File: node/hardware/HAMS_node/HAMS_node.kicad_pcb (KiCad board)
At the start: 2 copper layers, 76.1 x 40.1 mm, 41 parts, among them J1 Conn_01x02, J2 Conn_02x07_Odd_Even, J3 Conn_01x04, J4 Conn_01x04, J5 Conn_01x04, J6 Conn_01x04, J7 Conn_01x08, Q1 DMP3099L, SW1 TL3305BF100QG, SW2 TL3305BF100QG, U1 STM32L031K6Tx, U2 NRF24L01_Breakout, U3 nRF24L01p SMD module, Y1 CM9V-T1A

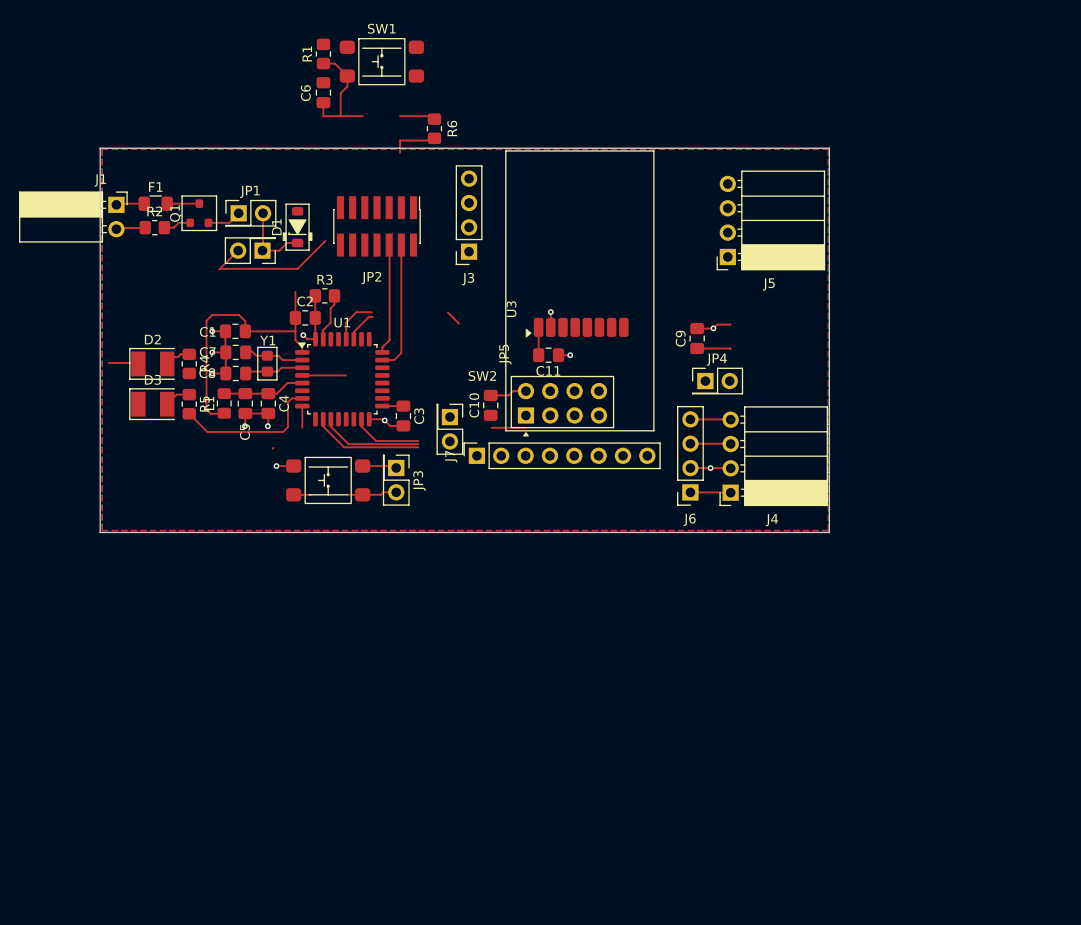
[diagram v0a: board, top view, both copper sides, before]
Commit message: Improve HAMS node HW: PCB and device resize
Change many 0805 devices for 0603 devices.
Add mounting holes.
Make the board 4.5 x 5 cm size.
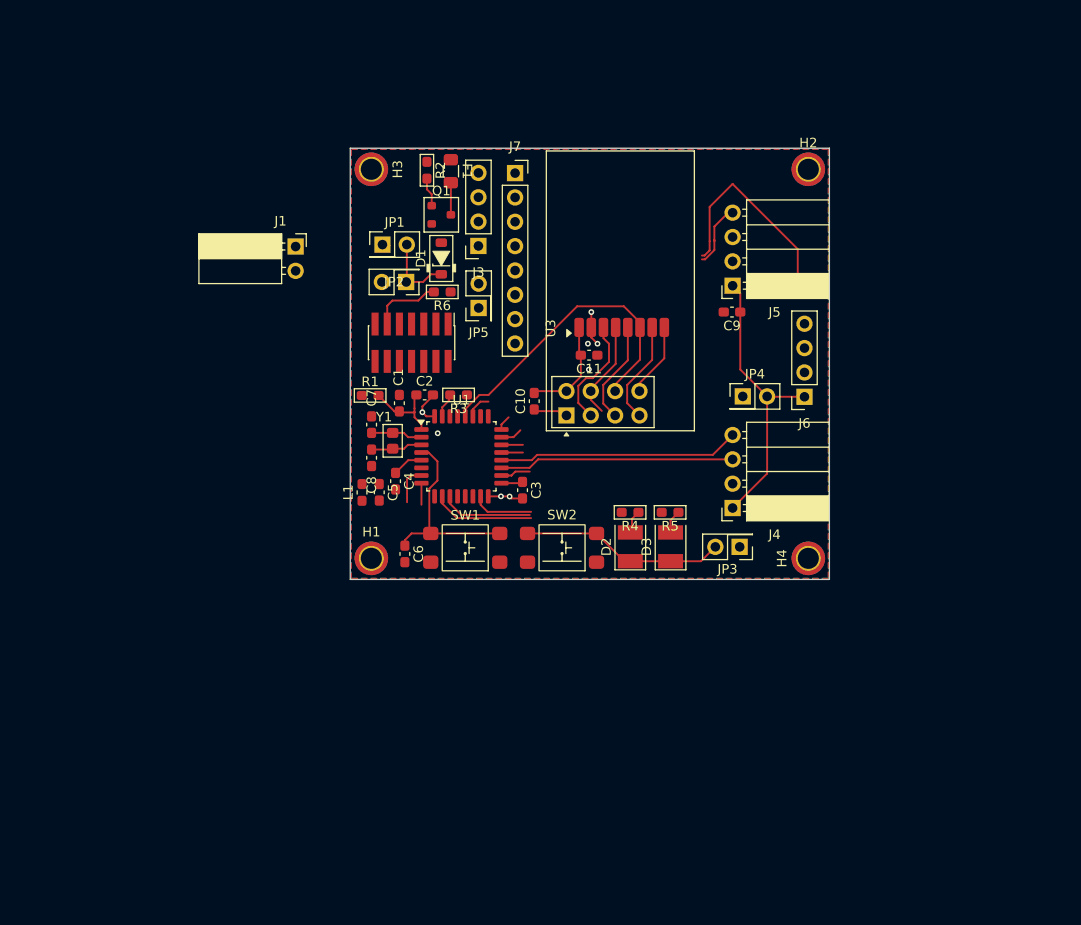
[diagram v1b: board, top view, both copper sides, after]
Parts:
- added H1: MountingHole_Pad, MountingHole:MountingHole_2.2mm_M2_ISO7380_Pad_TopBottom, F.Cu at (142.3, 71.4)
- added H2: MountingHole_Pad, MountingHole:MountingHole_2.2mm_M2_ISO7380_Pad_TopBottom, F.Cu at (187.9, 30.8)
- added H3: MountingHole_Pad, MountingHole:MountingHole_2.2mm_M2_ISO7380_Pad_TopBottom, F.Cu at (142.3, 30.8)
- added H4: MountingHole_Pad, MountingHole:MountingHole_2.2mm_M2_ISO7380_Pad_TopBottom, F.Cu at (187.9, 71.4)
- C1, C10, C11, C2, C3, C4, C5, C6, C7, C8, C9: footprint Capacitor_SMD:C_0805_2012Metric_Pad1.18x1.45mm_HandSolder -> Capacitor_SMD:C_0603_1608Metric_Pad1.08x0.95mm_HandSolder
- L1: footprint Inductor_SMD:L_0805_2012Metric_Pad1.15x1.40mm_HandSolder -> Inductor_SMD:L_0603_1608Metric_Pad1.05x0.95mm_HandSolder
- R1, R2, R3, R4, R5, R6: footprint Resistor_SMD:R_0805_2012Metric_Pad1.20x1.40mm_HandSolder -> PCM_Resistor_SMD_AKL:R_0603_1608Metric_Pad1.05x0.95mm_HandSolder
- moved D3 56.0 mm to (173.5, 70.2), turned to 90 degrees
- moved D2 53.4 mm to (169.3, 70.2), turned to 90 degrees
- moved SW1 51.5 mm to (152.1, 70.3), turned to 180 degrees
- moved R5 51.4 mm to (173.5, 66.6), turned to 180 degrees
- moved C6 48.9 mm to (145.8, 70.9), turned to -90 degrees
- moved R4 48.5 mm to (169.3, 66.6), turned to 180 degrees
- moved JP3 36.8 mm to (180.7, 70.2), turned to 180 degrees
- moved R1 36.0 mm to (142.2, 54.4), turned to 0 degrees
- moved F1 31.0 mm to (150.6, 31.0), turned to -90 degrees
- moved J7 29.8 mm to (157.3, 31.2), turned to 0 degrees
- moved R2 29.0 mm to (148.1, 30.9), turned to -90 degrees
- moved SW2 25.4 mm to (162.2, 70.3), turned to 180 degrees
- moved Q1 25.3 mm to (149.6, 35.5), turned to 0 degrees
- moved J1 19.2 mm to (134.4, 38.9)
- moved C1 18.7 mm to (145.2, 55.2), turned to 90 degrees
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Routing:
- net /I2C_SDA: track 4.21 -> 55.8 mm
- net GND: track 51.7 -> 14.9 mm, vias 12 -> 8
- net /VDD_MCU: track 46.0 -> 10.5 mm
- net /SPI_MOSI: track 4.87 -> 32.4 mm
- net /VDD_SENSOR: track 7.73 -> 30.1 mm
- net /I2C_SCL: track 4.21 -> 24.5 mm
- net /nRF24_CE: track 0.75 -> 15.6 mm
- net /LED_RED: track 15.6 -> 4.06 mm
- net Net-(D2-K): track 10.1 -> 21.4 mm
- net /SWDIO: track 13.6 -> 2.28 mm
- net /SPI_MISO: track 3.38 -> 13.5 mm
- net /SWCLK: track 11.5 -> 1.59 mm
- net /SPI_SCK: track 10.6 -> 20.3 mm
- net /nRF24_CSN: track 11.7 -> 20.9 mm
- net /nRF24_IRQ: track 7.31 -> 14.2 mm
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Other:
- board size 76.1 x 40.1 mm -> 50 x 45 mm

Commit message: Improve HAMS node HW: PCB resize, optimization
Optimize MCU pinout with respect to PCB routing.
Change PCB size to 47.5 mm x 50 mm.
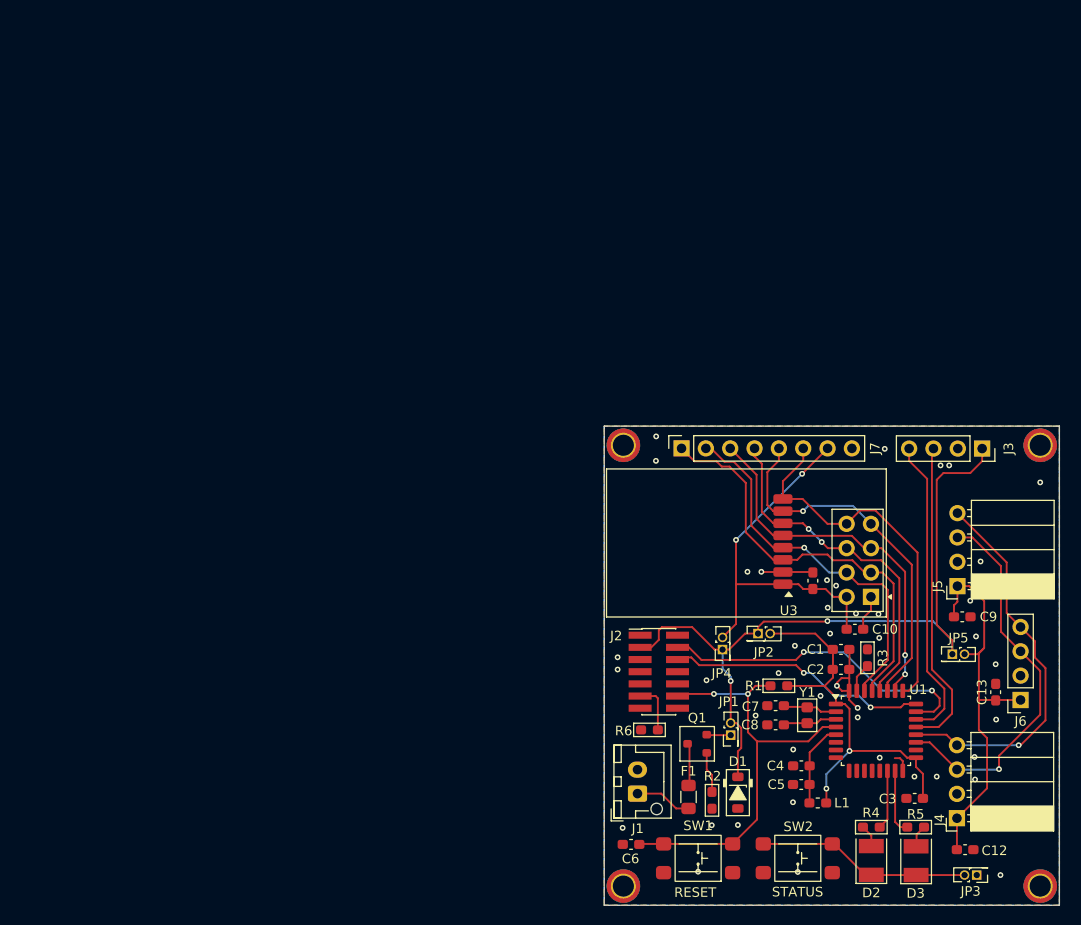
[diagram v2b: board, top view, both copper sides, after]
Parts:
- added C12: 10 uF, Capacitor_SMD:C_0603_1608Metric_Pad1.08x0.95mm_HandSolder, F.Cu at (204.3, 101.8)
- added C13: 10 uF, Capacitor_SMD:C_0603_1608Metric_Pad1.08x0.95mm_HandSolder, F.Cu at (207.4, 85.4)
- J1: footprint Connector_PinSocket_2.54mm:PinSocket_1x02_P2.54mm_Horizontal -> Connector_JST:JST_XH_B2B-XH-AM_1x02_P2.50mm_Vertical
- JP1, JP2, JP3: footprint Connector_PinHeader_2.54mm:PinHeader_2x01_P2.54mm_Vertical -> Connector_PinHeader_1.27mm:PinHeader_2x01_P1.27mm_Vertical
- JP4: renamed from JP5; footprint Connector_PinHeader_2.54mm:PinHeader_2x01_P2.54mm_Vertical -> Connector_PinHeader_1.27mm:PinHeader_2x01_P1.27mm_Vertical
- JP5: renamed from JP4; footprint Connector_PinHeader_2.54mm:PinHeader_2x01_P2.54mm_Vertical -> Connector_PinHeader_1.27mm:PinHeader_2x01_P1.27mm_Vertical
- Y1: footprint PCM_Crystal_Handsoldering_AKL:Crystal_SMD_MicroCrystal_CM9V-T1A-2Pin_1.6x1.0mm_BigPads -> PCM_Crystal_AKL:Crystal_SMD_MicroCrystal_CM9V-T1A-2Pin_1.6x1.0mm_BigPads
- moved H2 78.6 mm to (212.1, 105.6), turned to 45 degrees
- moved H3 75.5 mm to (212.1, 59.6), turned to 45 degrees
- moved R2 72.2 mm to (177.8, 96.7), turned to 90 degrees
- moved F1 69.9 mm to (175.4, 96.3), turned to 90 degrees
- moved J1 67.3 mm to (170.1, 96.0), turned to 90 degrees
- moved D1 63.8 mm to (180.6, 95.8), turned to -90 degrees
- moved JP1 62.8 mm to (179.8, 89.8), turned to 90 degrees
- moved Q1 61.3 mm to (176.3, 90.8), turned to 180 degrees
- moved L1 57.6 mm to (188.9, 96.9), turned to 180 degrees
- moved J3 56.7 mm to (206.0, 59.9), turned to -90 degrees
- moved C5 53.6 mm to (187.2, 95.0), turned to 180 degrees
- moved C1 52.8 mm to (191.3, 80.9), turned to 0 degrees
- moved R1 52.3 mm to (184.8, 84.7)
- moved C3 52.1 mm to (199.0, 96.5), turned to 180 degrees
- moved C2 52.0 mm to (191.3, 83.0)
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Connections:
- J7 pad 1: /nRF24_CSN -> /nRF24_CE
- J7 pad 2: /nRF24_CE -> /nRF24_CSN
- J7 pad 3: /nRF24_IRQ -> /SPI_SCK
- J7 pad 4: /SPI_SCK -> /SPI_MOSI
- J7 pad 6: /SPI_MOSI -> /nRF24_IRQ
- U1 pad 10: /nRF24_CSN -> unconnected-(U1-PA4-Pad10)
- U1 pad 11: /SPI_SCK -> unconnected-(U1-PA5-Pad11)
- U1 pad 14: unconnected-(U1-PB0-Pad14) -> /LED_GREEN
- U1 pad 15: /nRF24_IRQ -> /LED_RED
- U1 pad 18: /nRF24_CE -> unconnected-(U1-PA8-Pad18)
- U1 pad 25: unconnected-(U1-PA15-Pad25) -> /nRF24_IRQ
- U1 pad 26: unconnected-(U1-PB3-Pad26) -> /SPI_SCK
- U1 pad 29: unconnected-(U1-PB6-Pad29) -> /nRF24_CE
- U1 pad 30: unconnected-(U1-PB7-Pad30) -> /nRF24_CSN
- U1 pad 7: /LED_RED -> unconnected-(U1-PA1-Pad7)
- U1 pad 8: /LED_GREEN -> unconnected-(U1-PA2-Pad8)
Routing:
- net VDD: track 7.92 -> 79.4 mm, vias 0 -> 2
- net /SWDIO: track 2.28 -> 34.4 mm, vias 0 -> 2
- net /VDD_MCU: track 10.5 -> 41.9 mm, vias 0 -> 2
- net /GPIO_0: track 2.24 -> 32.9 mm
- net /GPIO_1: track 2.24 -> 32.1 mm
- net /VDD_nRF24: track 10.9 -> 39.4 mm, vias 0 -> 2
- net /nRF24_CE: track 15.6 -> 43.6 mm
- net /SWCLK: track 1.59 -> 27.7 mm, vias 0 -> 2
- net /NRST: track 20.8 -> 46.1 mm, vias 0 -> 2
- net /SPI_MISO: track 13.5 -> 38.7 mm, vias 0 -> 1
- net /nRF24_IRQ: track 14.2 -> 39.4 mm
- net /SPI_SCK: track 20.3 -> 39.1 mm, vias 0 -> 2
- net /nRF24_CSN: track 20.9 -> 39.5 mm, vias 0 -> 1
- net /I2C_SCL: track 24.5 -> 40.4 mm, vias 0 -> 1
- net /I2C_SDA: track 55.8 -> 40.5 mm, vias 0 -> 1
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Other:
- board size 50 x 45 mm -> 47.5 x 50 mm
- board text added: "RESET"
- board text added: "STATUS"

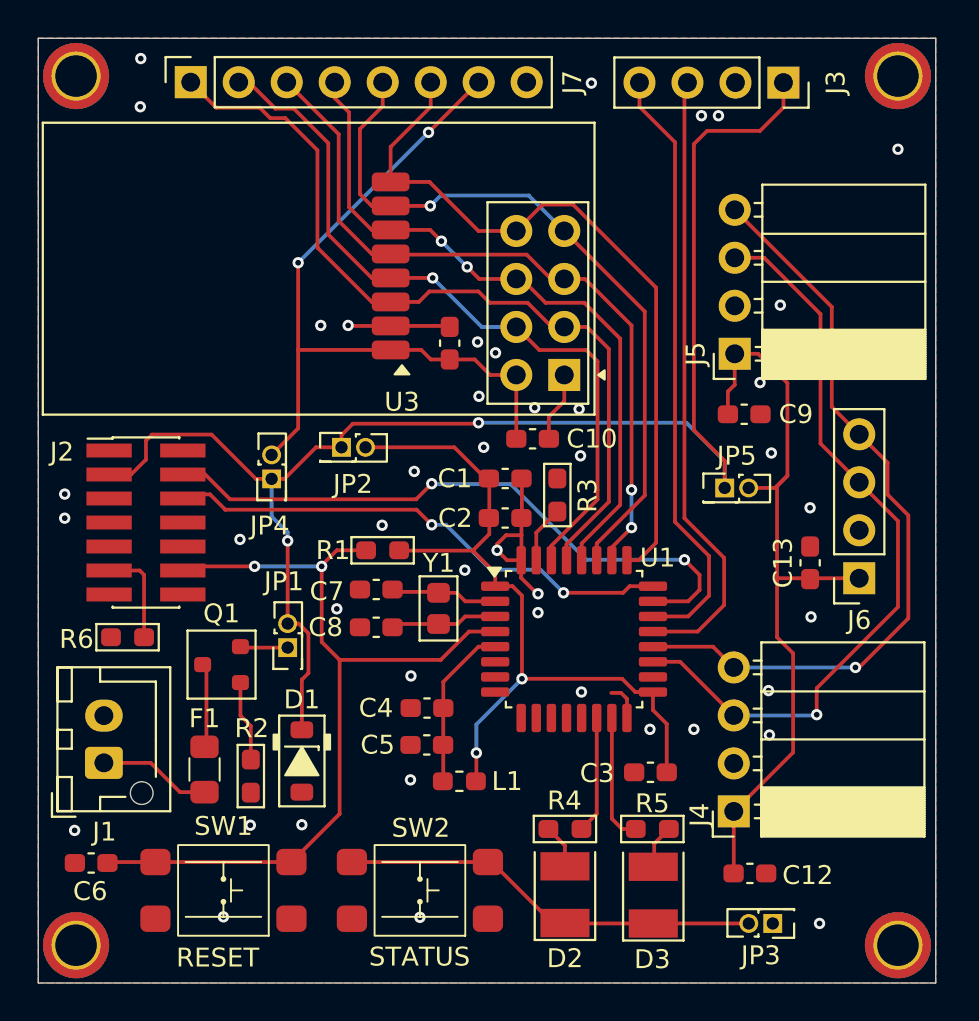
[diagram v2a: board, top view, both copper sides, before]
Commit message: Improve HAMS node HW: schematic and PCB
Change LED section (compact LED, DPDT switch).
Remove VDDA ferrite bead and bulk capacitor.
Add pads for I2C pullups.
Add silkscreen labels.
Update footprints of custom symbols.
Change mounting holes to non-grounded.
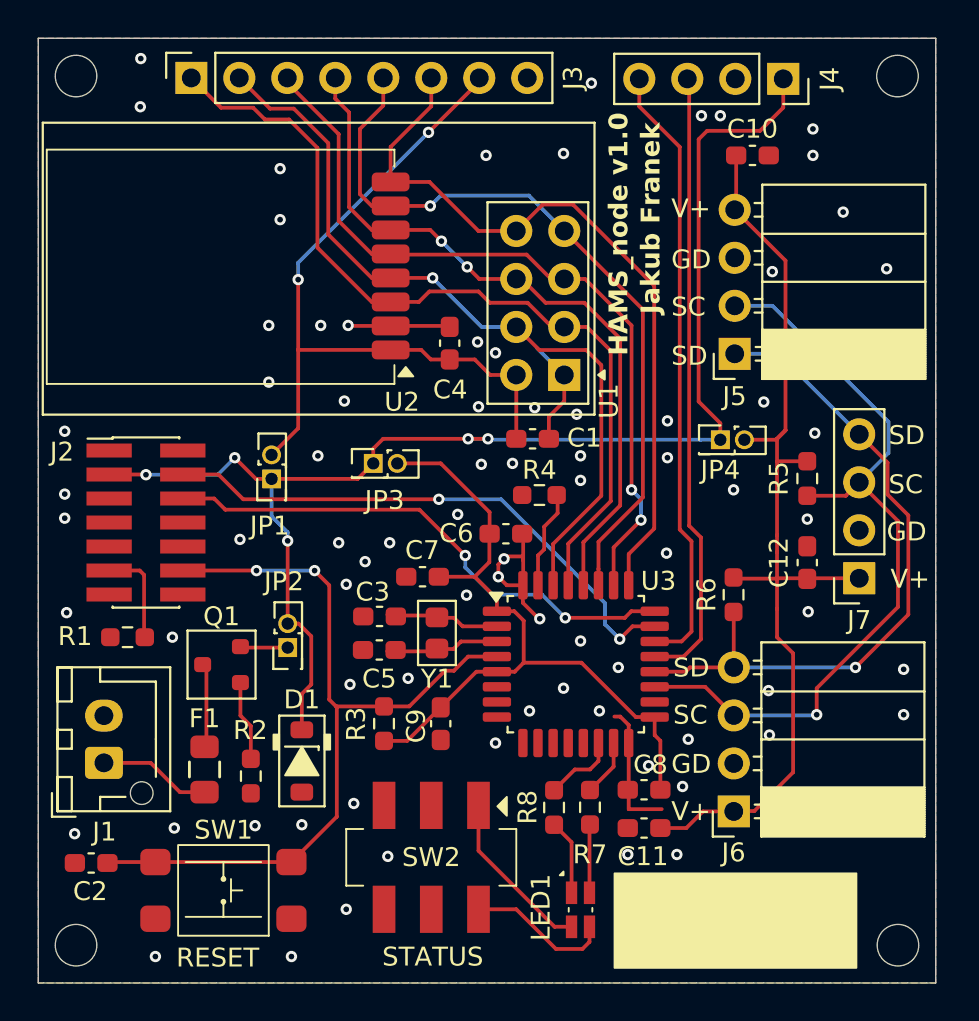
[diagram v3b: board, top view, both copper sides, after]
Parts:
- removed the C5 at (187.2, 95.0)
- removed D2: VLMC3101, LED_SMD:LED_PLCC-2_3.4x3.0mm_KA
- removed D3: VLMS30K1L2, LED_SMD:LED_PLCC-2_3.4x3.0mm_KA
- removed the JP3 at (205.5, 104.5)
- removed L1: 600 Ohm bead, Inductor_SMD:L_0603_1608Metric_Pad1.05x0.95mm_HandSolder
- added LED1: APHBM2012LSURKCGKC, Personal_SamacSys:KPHBM2012QBDCGKC, F.Cu at (195.3, 103.6)
- added R5: 10 kOhm, Resistor_SMD:R_0603_1608Metric_Pad0.98x0.95mm_HandSolder, F.Cu at (207.3, 80.9)
- added R6: 10 kOhm, Resistor_SMD:R_0603_1608Metric_Pad0.98x0.95mm_HandSolder, F.Cu at (203.4, 87.0)
- H1, H2, H3, H4: value MountingHole_Pad -> MountingHole; footprint MountingHole:MountingHole_2.2mm_M2_ISO7380_Pad_TopBottom -> MountingHole:MountingHole_2.2mm_M2_ISO7380
- R1: renamed from R6; footprint PCM_Resistor_SMD_AKL:R_0603_1608Metric_Pad1.05x0.95mm_HandSolder -> Resistor_SMD:R_0603_1608Metric_Pad0.98x0.95mm_HandSolder
- R2: footprint PCM_Resistor_SMD_AKL:R_0603_1608Metric_Pad1.05x0.95mm_HandSolder -> Resistor_SMD:R_0603_1608Metric_Pad0.98x0.95mm_HandSolder
- R3: renamed from R1; footprint PCM_Resistor_SMD_AKL:R_0603_1608Metric_Pad1.05x0.95mm_HandSolder -> Resistor_SMD:R_0603_1608Metric_Pad0.98x0.95mm_HandSolder
- R4: renamed from R3; footprint PCM_Resistor_SMD_AKL:R_0603_1608Metric_Pad1.05x0.95mm_HandSolder -> Resistor_SMD:R_0603_1608Metric_Pad0.98x0.95mm_HandSolder
- R7: renamed from R4; value 700 Ohm -> 680 Ohm; footprint PCM_Resistor_SMD_AKL:R_0603_1608Metric_Pad1.05x0.95mm_HandSolder -> Resistor_SMD:R_0603_1608Metric_Pad0.98x0.95mm_HandSolder
- R8: renamed from R5; value 750 Ohm -> 680 Ohm; footprint PCM_Resistor_SMD_AKL:R_0603_1608Metric_Pad1.05x0.95mm_HandSolder -> Resistor_SMD:R_0603_1608Metric_Pad0.98x0.95mm_HandSolder
- SW2: value TL3305BF100QG -> JS202011SCQN; footprint Personal_Switches:E-Switch_TL3305BF100QG_Tactile_SPST -> Personal_SamacSys:JS202011SCQN
- moved H2 63.3 mm to (168.6, 59.6), turned to 0 degrees
- moved H4 63.3 mm to (212.1, 59.6), turned to 0 degrees
- moved H1 46.0 mm to (168.6, 105.6), turned to 0 degrees
- moved H3 46.0 mm to (212.1, 105.6), turned to 0 degrees
- moved C10 13.7 mm to (204.4, 63.8)
- moved R3 9.18 mm to (184.9, 93.9), turned to -90 degrees
- moved C11 6.09 mm to (198.7, 99.4), turned to 180 degrees
- moved C7 5.36 mm to (186.9, 86.1), turned to 180 degrees
- moved R8 5.32 mm to (193.9, 98.3), turned to 90 degrees
- moved C6 2.93 mm to (191.3, 83.8)
- moved JP4 2.56 mm to (202.7, 78.8)
- moved JP3 1.88 mm to (184.3, 80.1)
- moved SW2 1.85 mm to (187.4, 101.0)
- moved R7 1.75 mm to (195.8, 98.3), turned to 90 degrees
- moved C3 1.44 mm to (184.7, 88.2)
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- renumbered C10 to C1, C9 to C10, C12 to C11, C13 to C12, C6 to C2, C7 to C3, C11 to C4, C8 to C5, C1 to C6, C2 to C7, C3 to C8, C4 to C9, J7 to J3, J3 to J4, J4 to J6, J6 to J7, JP4 to JP1, JP1 to JP2, JP2 to JP3, JP5 to JP4, U2 to U1, U3 to U2, U1 to U3
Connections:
- C9 pad 1: /VDDA_MCU -> /VDD_MCU
- J5 pad 1: /VDD_SENSOR -> /I2C_SDA
- J5 pad 2: GND -> /I2C_SCL
- J5 pad 3: /I2C_SCL -> GND
- J5 pad 4: /I2C_SDA -> /VDD_SENSOR
- SW2 pad 1: GND -> Net-(LED1-CATHODE_RED)
- SW2 pad 2: Net-(D2-K) -> GND
- U3 pad 14: /LED_GREEN -> /LED_RED
- U3 pad 15: /LED_RED -> /LED_GREEN
- U3 pad 5: /VDDA_MCU -> /VDD_MCU
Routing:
- net Net-(D2-K): track 22.4 -> 0.00 mm
- net /VDD_SENSOR: track 41.3 -> 52.6 mm
- net Net-(LED1-CATHODE_RED): track 0.00 -> 8.74 mm
- net /VDDA_MCU: track 8.39 -> 0.00 mm
- net Net-(LED1-CATHODE_GREEN): track 0.00 -> 7.70 mm
- net VDD: track 79.4 -> 73.4 mm, vias 2 -> 5
- net GND: track 20.6 -> 26.1 mm, vias 43 -> 78
- net /SWDIO: track 34.4 -> 29.9 mm
- net /I2C_SDA: track 40.5 -> 36.8 mm
- net /LED_GREEN: track 6.21 -> 3.01 mm
- net /NRST: track 46.1 -> 43.0 mm
- net /VDD_MCU: track 41.9 -> 38.9 mm, vias 2 -> 0
- net /LED_RED: track 6.82 -> 3.94 mm
- net /SPI_SCK: track 39.1 -> 41.7 mm
- net /BOOT0: track 3.04 -> 5.20 mm
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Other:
- board text added: "GD"
- board text added: "GND"
- board text added: "GPIO_0"
- board text added: "GPIO_1"
- board text added: "HAMS_node v1.0"
- board text added: "JLCJLCJLCJLC"
- board text added: "Jakub Franek"
- board text added: "SC"
- board text added: "SD"
- board text added: "SPI_MISO"
- board text added: "SPI_MOSI"
- board text added: "SPI_SCK"
- board text added: "V+"
- board text added: "VBAT"
- board text added: "VDD"
- board text added: "VDD_nRF24"
- board text added: "nRF24_CE"
- board text added: "nRF24_CSN"
- board text added: "nRF24_IRQ"
